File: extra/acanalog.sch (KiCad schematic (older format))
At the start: 20 parts, among them P7 belaaudioout, P8 belaaudioin, P9 mod_ac-io, U1 TL074

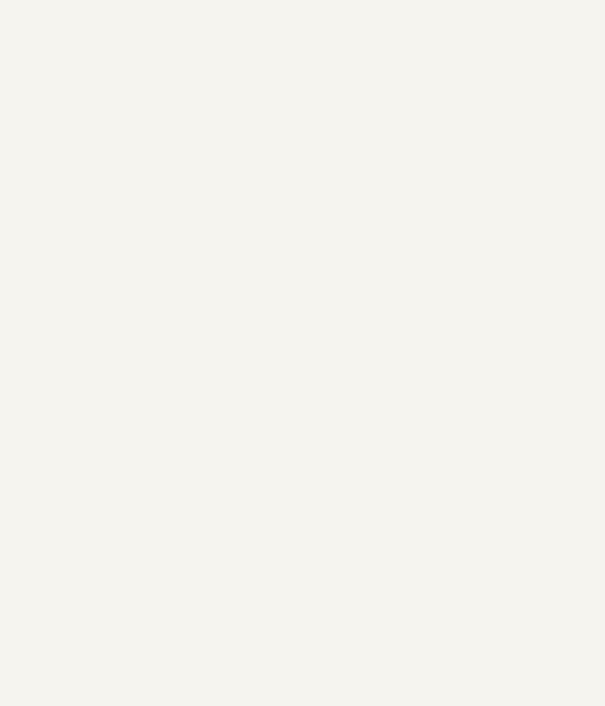
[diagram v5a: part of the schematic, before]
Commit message: added decoupling caps, power expand, more layout
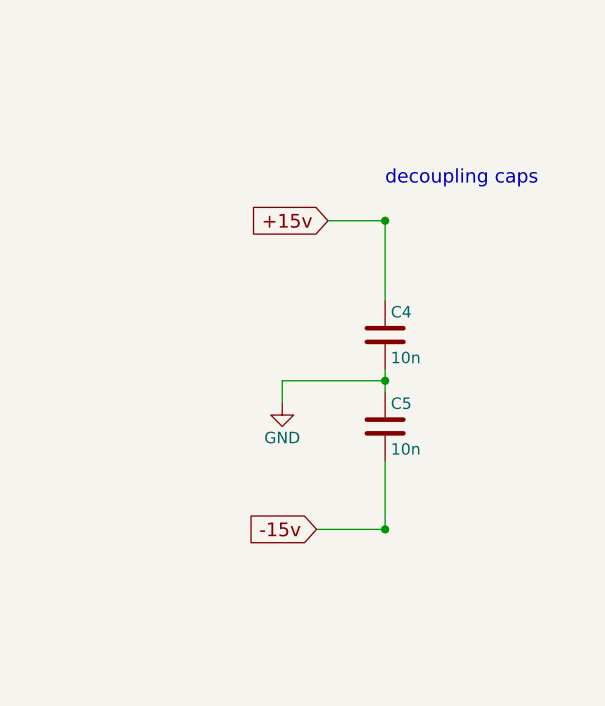
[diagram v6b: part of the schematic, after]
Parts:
- added C4, C5: 10n, Capacitors_ThroughHole:C_Rect_L4_W2.5_P2.5, symbol C
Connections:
- net +15v: now also C4.1
- net -15v: now also C5.2
- net GND: now also C4.2, C5.1
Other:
- note added: "decoupling caps"
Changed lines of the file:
@@
 Connection ~ 2300 2050
 $Comp
-L GND #PWR010
+L GND #PWR7
 U 1 1 5857538D
 P 2450 1750
-F 0 "#PWR010" H 2450 1500 50  0001 C CNN
+F 0 "#PWR7" H 2450 1500 50  0001 C CNN
 F 1 "GND" H 2450 1600 50  0000 C CNN
 F 2 "" H 2450 1750 50  0000 C CNN
@@
 Connection ~ 2300 3400
 $Comp
-L GND #PWR011
+L GND #PWR8
 U 1 1 585753C3
 P 2450 3100
-F 0 "#PWR011" H 2450 2850 50  0001 C CNN
+F 0 "#PWR8" H 2450 2850 50  0001 C CNN
 F 1 "GND" H 2450 2950 50  0000 C CNN
 F 2 "" H 2450 3100 50  0000 C CNN
@@
 Connection ~ 2300 4850
 $Comp
-L GND #PWR012
+L GND #PWR9
 U 1 1 585753F9
 P 2450 4550
-F 0 "#PWR012" H 2450 4300 50  0001 C CNN
+F 0 "#PWR9" H 2450 4300 50  0001 C CNN
 F 1 "GND" H 2450 4400 50  0000 C CNN
 F 2 "" H 2450 4550 50  0000 C CNN
@@
 Connection ~ 4400 4750
 $Comp
-L GND #PWR013
+L GND #PWR11
 U 1 1 58575424
 P 4400 5300
-F 0 "#PWR013" H 4400 5050 50  0001 C CNN
+F 0 "#PWR11" H 4400 5050 50  0001 C CNN
 F 1 "GND" H 4400 5150 50  0000 C CNN
 F 2 "" H 4400 5300 50  0000 C CNN
@@
 Connection ~ 2300 6200
 $Comp
-L GND #PWR014
+L GND #PWR10
 U 1 1 58575447
 P 2450 5900
-F 0 "#PWR014" H 2450 5650 50  0001 C CNN
+F 0 "#PWR10" H 2450 5650 50  0001 C CNN
 F 1 "GND" H 2450 5750 50  0000 C CNN
 F 2 "" H 2450 5900 50  0000 C CNN
@@
 Connection ~ 4400 6100
 $Comp
-L GND #PWR015
+L GND #PWR12
 U 1 1 58575472
 P 4400 6650
-F 0 "#PWR015" H 4400 6400 50  0001 C CNN
+F 0 "#PWR12" H 4400 6400 50  0001 C CNN
 F 1 "GND" H 4400 6500 50  0000 C CNN
 F 2 "" H 4400 6650 50  0000 C CNN
@@
 	1450 1350 1400 1350
 $Comp
-L GND #PWR016
+L GND #PWR6
 U 1 1 58575BEC
 P 1550 1550
-F 0 "#PWR016" H 1550 1300 50  0001 C CNN
+F 0 "#PWR6" H 1550 1300 50  0001 C CNN
 F 1 "GND" H 1550 1400 50  0000 C CNN
 F 2 "" H 1550 1550 50  0000 C CNN
@@
 belaacin2
 $Comp
-L GND #PWR017
+L GND #PWR13
 U 1 1 58575F21
 P 4700 1450
-F 0 "#PWR017" H 4700 1200 50  0001 C CNN
+F 0 "#PWR13" H 4700 1200 50  0001 C CNN
 F 1 "GND" H 4700 1300 50  0000 C CNN
 F 2 "" H 4700 1450 50  0000 C CNN
@@
 	6350 3350 6150 3350
 $Comp
-L GND #PWR018
+L GND #PWR14
 U 1 1 58576B81
 P 6900 3400
-F 0 "#PWR018" H 6900 3150 50  0001 C CNN
+F 0 "#PWR14" H 6900 3150 50  0001 C CNN
 F 1 "GND" H 6900 3250 50  0000 C CNN
 F 2 "" H 6900 3400 50  0000 C CNN
@@
 Connection ~ 6900 3150
 Connection ~ 6900 3250
+$Comp
+L C C4
+U 1 1 5871BD68
+P 9450 3450
+F 0 "C4" H 9475 3550 50  0000 L CNN
+F 1 "10n" H 9475 3350 50  0000 L CNN
+F 2 "Capacitors_ThroughHole:C_Rect_L4_W2.5_P2.5" H 9488 3300 50  0001 C CNN
+F 3 "" H 9450 3450 50  0000 C CNN
+	1    9450 3450
+	1    0    0    -1
+$EndComp
+$Comp
+L C C5
+U 1 1 5871BD6F
+P 9450 3850
+F 0 "C5" H 9475 3950 50  0000 L CNN
+F 1 "10n" H 9475 3750 50  0000 L CNN
+F 2 "Capacitors_ThroughHole:C_Rect_L4_W2.5_P2.5" H 9488 3700 50  0001 C CNN
+F 3 "" H 9450 3850 50  0000 C CNN
+	1    9450 3850
+	1    0    0    -1
+$EndComp
+Text GLabel 9200 2950 0    60   Input ~ 0
++15v
+Text GLabel 9150 4300 0    60   Input ~ 0
+-15v
+$Comp
+L GND #PWR15
+U 1 1 5871BD94
+P 9000 3750
+F 0 "#PWR15" H 9000 3500 50  0001 C CNN
+F 1 "GND" H 9000 3600 50  0000 C CNN
+F 2 "" H 9000 3750 50  0000 C CNN
+F 3 "" H 9000 3750 50  0000 C CNN
+	1    9000 3750
+	1    0    0    -1
+$EndComp
+Text Notes 9450 2800 0    60   ~ 0
+decoupling caps
+Wire Wire Line
+	9450 3600 9450 3700
+Connection ~ 9450 3650
+Wire Wire Line
+	9450 2950 9450 3300
+Wire Wire Line
+	9450 4000 9450 4300
+Wire Wire Line
+	9000 3750 9000 3650
+Connection ~ 9450 4300
+Connection ~ 9450 2950
+Wire Wire Line
+	9450 2950 9200 2950
+Wire Wire Line
+	9000 3650 9450 3650
+Wire Wire Line
+	9450 4300 9150 4300
 $EndSCHEMATC
